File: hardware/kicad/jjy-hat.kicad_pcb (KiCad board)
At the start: 2 copper layers, 65 x 56 mm, 26 parts, among them J1 GPIO 2x20 stacking header, J2 Antenna, K1 AQY212SX, U1 74LVC125, U2 DS3231SN#

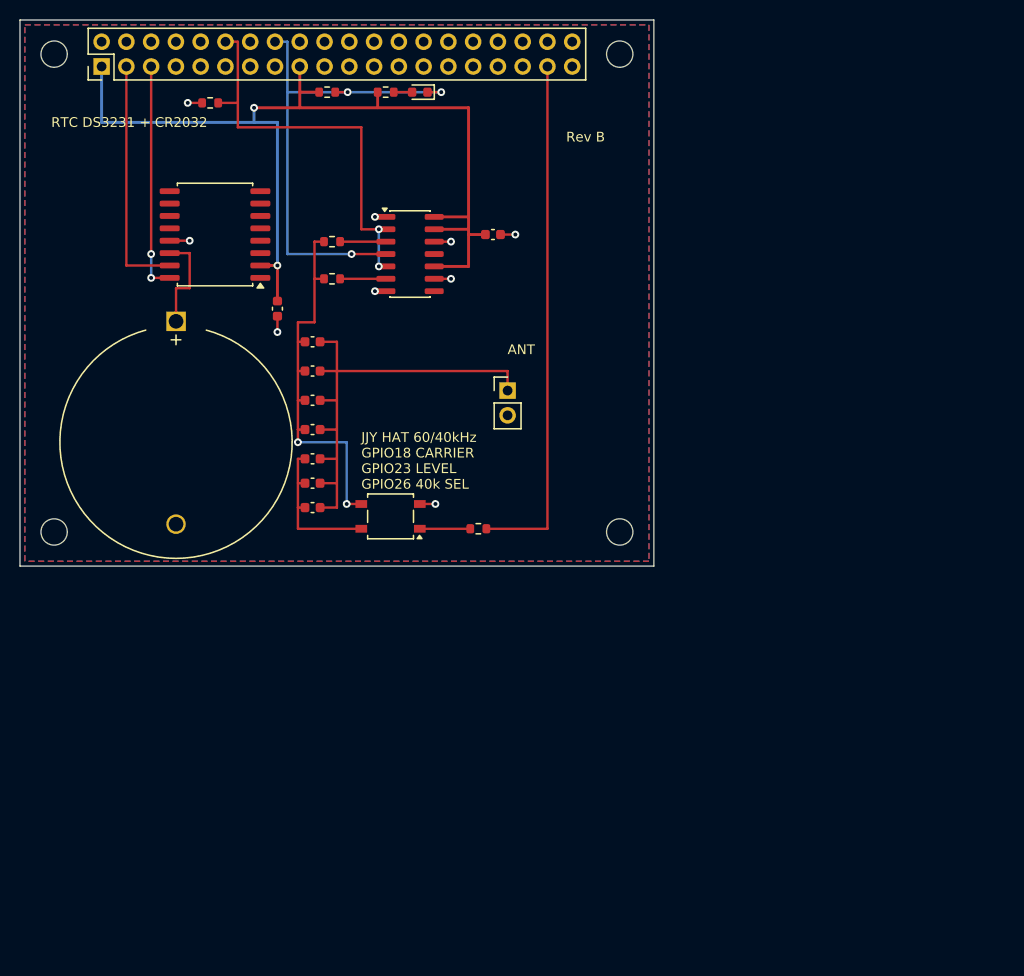
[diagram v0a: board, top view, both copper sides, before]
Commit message: Rev C board: LCD, LEDs, PCB spiral antenna, antenna select, optional resonance
- Leaded R/LED/C parts (hand-soldered); only U1/U2 are SMT at JLCPCB
- 16x2 I2C LCD (J3) shows current time; signal LED (low-level period),
  level LED and power pilot LED grouped at the board's top-left
- Antenna is an on-board PCB spiral coil; JP1 selects it or external J2
- Optional (DNP) resonance bank + K1 40/60kHz switch for external coils
- J1 at top-center, board 100x96 mm to fit the metal case via a cable
- jjyd: LCD driver, signal LED, optional select_gpio, DS3231 RTC support
- Regenerated Gerber/BOM/CPL and updated docs

Co-Authored-By: Claude Sonnet 5.5 <noreply@anthropic.com>
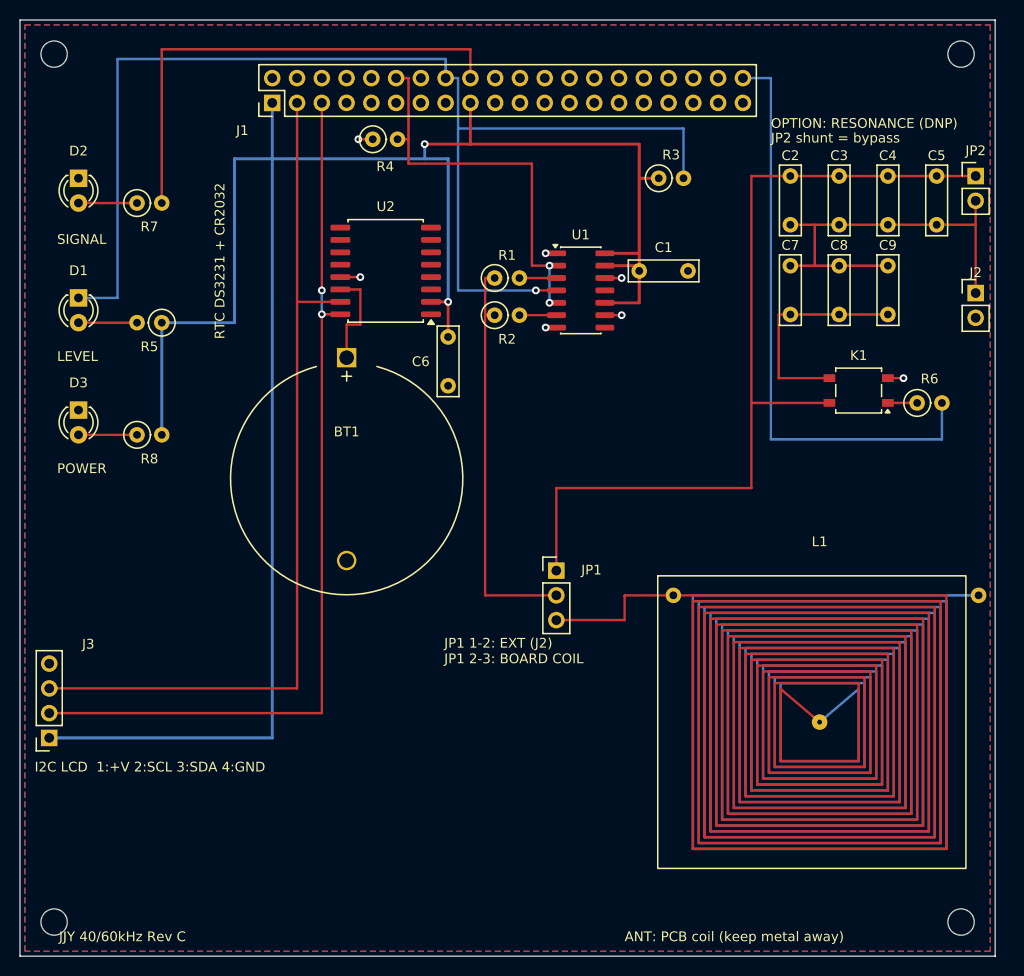
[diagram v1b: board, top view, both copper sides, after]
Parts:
- added D2: LED green, LED_THT:LED_D3.0mm, F.Cu at (6.00, 16.2)
- added D3: LED yellow, LED_THT:LED_D3.0mm, F.Cu at (6.00, 40.0)
- added J3: I2C LCD (AE-AQM1602A), Connector_PinSocket_2.54mm:PinSocket_1x04_P2.54mm_Vertical, F.Cu at (3.00, 73.6)
- added JP1: Antenna select, Connector_PinHeader_2.54mm:PinHeader_1x03_P2.54mm_Vertical, F.Cu at (55.0, 56.5)
- added JP2: Resonance bypass, Connector_PinHeader_2.54mm:PinHeader_1x02_P2.54mm_Vertical, F.Cu at (98.0, 16.0)
- added L1: PCB spiral coil, JJY:Coil_Spiral, F.Cu at (82.0, 72.0)
- added R7: 330, Resistor_THT:R_Axial_DIN0207_L6.3mm_D2.5mm_P2.54mm_Vertical, F.Cu at (12.0, 18.8)
- added R8: 470, Resistor_THT:R_Axial_DIN0207_L6.3mm_D2.5mm_P2.54mm_Vertical, F.Cu at (12.0, 42.5)
- C1, C5, C6: footprint Capacitor_SMD:C_0603_1608Metric -> Capacitor_THT:C_Rect_L7.0mm_W2.0mm_P5.00mm
- C2, C7: value 4.7n C0G -> 4.7n C0G (DNP); footprint Capacitor_SMD:C_0603_1608Metric -> Capacitor_THT:C_Rect_L7.0mm_W2.0mm_P5.00mm
- C3, C8, C9: value 2.2n C0G -> 2.2n C0G (DNP); footprint Capacitor_SMD:C_0603_1608Metric -> Capacitor_THT:C_Rect_L7.0mm_W2.0mm_P5.00mm
- C4: value 150p C0G -> 150p C0G (DNP); footprint Capacitor_SMD:C_0603_1608Metric -> Capacitor_THT:C_Rect_L7.0mm_W2.0mm_P5.00mm
- D1: footprint LED_SMD:LED_0603_1608Metric -> LED_THT:LED_D3.0mm
- J1: value GPIO 2x20 stacking header -> GPIO 2x20 pin header (ribbon / Dupont)
- J2: value Antenna -> External antenna
- K1: value AQY212SX -> AQY212SX (DNP)
- R1: value 1k -> 10k; footprint Resistor_SMD:R_0603_1608Metric -> Resistor_THT:R_Axial_DIN0207_L6.3mm_D2.5mm_P2.54mm_Vertical
- R2: value 100 -> 1.1k; footprint Resistor_SMD:R_0603_1608Metric -> Resistor_THT:R_Axial_DIN0207_L6.3mm_D2.5mm_P2.54mm_Vertical
- R3, R4, R5: footprint Resistor_SMD:R_0603_1608Metric -> Resistor_THT:R_Axial_DIN0207_L6.3mm_D2.5mm_P2.54mm_Vertical
- R6: value 330 -> 330 (DNP); footprint Resistor_SMD:R_0603_1608Metric -> Resistor_THT:R_Axial_DIN0207_L6.3mm_D2.5mm_P2.54mm_Vertical
- moved C5 69.1 mm to (94.0, 16.0), turned to 270 degrees
- moved C4 63.3 mm to (89.0, 16.0), turned to 270 degrees
- moved C9 62.2 mm to (89.0, 30.2), turned to 90 degrees
- moved C3 57.6 mm to (84.0, 16.0), turned to 270 degrees
- moved C8 56.7 mm to (84.0, 30.2), turned to 90 degrees
- moved H4 53.2 mm to (96.5, 92.5)
- moved C2 51.9 mm to (79.0, 16.0), turned to 270 degrees
- moved C7 51.2 mm to (79.0, 30.2), turned to 90 degrees
- moved K1 49.7 mm to (86.0, 38.0)
- moved J2 49.0 mm to (98.0, 28.0)
- moved R6 46.8 mm to (92.0, 39.3)
- moved D1 40.9 mm to (6.00, 28.5), turned to 270 degrees
- moved H3 40.0 mm to (3.50, 92.5)
- moved R3 35.1 mm to (65.5, 16.2)
- moved H2 35.0 mm to (96.5, 3.50)
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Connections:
- net /ANT renamed /ANT_X
- C2 pad 1: /DRV -> /EXT_IN
- C3 pad 1: /DRV -> /EXT_IN
- C4 pad 1: /DRV -> /EXT_IN
- C5 pad 1: /DRV -> /EXT_IN
- J1 pad 18: unconnected-(J1-Pin_18-Pad18) -> /SIGLED
- J1 pad 37: /FSEL -> unconnected-(J1-Pin_37-Pad37)
- J1 pad 40: unconnected-(J1-Pin_40-Pad40) -> /FSEL
- K1 pad 3: /DRV -> /CSW
- K1 pad 4: /CSW -> /EXT_IN
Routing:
- net +3V3: track 103.7 -> 222.3 mm
- net /EXT_IN: track 0.00 -> 91.5 mm
- net /LEVEL: track 51.6 -> 125.5 mm, vias 3 -> 1
- net /I2C_SCL: track 23.6 -> 92.4 mm
- net /I2C_SDA: track 24.8 -> 89.9 mm
- net /SIGLED: track 0.00 -> 50.4 mm
- net /ANT_B: track 0.00 -> 14.5 mm
- net /FSEL: track 53.7 -> 61.2 mm
- net /CSW: track 15.8 -> 22.9 mm
- net /SIGLED_A: track 0.00 -> 6.00 mm
- net /PWR_A: track 0.00 -> 6.00 mm
- net /ANT_X: track 48.6 -> 42.7 mm
- net /LED_A: track 1.89 -> 6.00 mm
- net GND: track 14.0 -> 10.8 mm, vias 9 -> 7
- net /RLY_A: track 5.17 -> 3.00 mm
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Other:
- board size 65 x 56 mm -> 100 x 96 mm
- board text added: "ANT: PCB coil (keep metal away)"
- board text added: "I2C LCD 1:+V 2:SCL 3:SDA 4:GND"
- board text added: "JJY 40/60kHz Rev C"
- board text added: "JP1 1-2: EXT (J2)"
- board text added: "JP1 2-3: BOARD COIL"
- board text added: "JP2 shunt = bypass"
- board text added: "LEVEL"
- board text added: "OPTION: RESONANCE (DNP)"
- board text added: "POWER"
- board text added: "SIGNAL"
- board text removed: "ANT"
- board text removed: "GPIO18 CARRIER"
- board text removed: "GPIO23 LEVEL"
- board text removed: "GPIO26 40k SEL"
- board text removed: "JJY HAT 60/40kHz"
- board text removed: "Rev B"

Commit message: Assemble K1 at JLCPCB and list DNP parts in the full BOM
- K1 (AQY212SX, C719754) is now an SMT part in the JLCPCB BOM/CPL
- Full BOM keeps DNP parts (C2-C5, C7-C9, R6) with a DNP column
- Docs updated accordingly; Gerber/BOM/CPL regenerated

Co-Authored-By: Claude Sonnet 5.5 <noreply@anthropic.com>
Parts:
- K1: value AQY212SX (DNP) -> AQY212SX
